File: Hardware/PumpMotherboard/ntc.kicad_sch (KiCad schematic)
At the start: 2 parts, among them J3 T_SENSOR

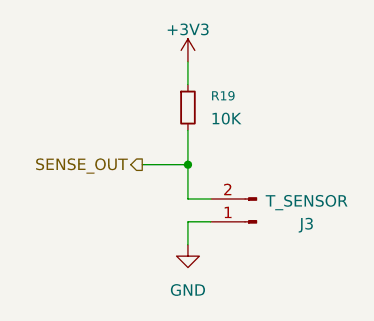
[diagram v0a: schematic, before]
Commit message: Fix DRC and ERC and add AGND
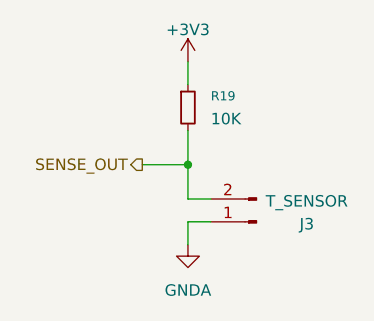
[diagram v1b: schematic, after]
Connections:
- net GND renamed GNDA
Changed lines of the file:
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@@
-	)
-	(symbol
-		(lib_id "power:GND")
-		(at 143.51 118.11 0)
-		(unit 1)
-		(body_style 1)
-		(exclude_from_sim no)
-		(in_bom yes)
-		(on_board yes)
-		(in_pos_files yes)
-		(dnp no)
-		(fields_autoplaced yes)
-		(property "Reference" "#PWR047"
-			(at 143.51 124.46 0)
-			(hide yes)
-			(show_name no)
-			(do_not_autoplace no)
-			(effects
-				(font
-					(size 1.27 1.27)
-				)
-			)
-		)
-		(property "Value" "GND"
-			(at 143.51 123.19 0)
-			(show_name no)
-			(do_not_autoplace no)
-			(effects
-				(font
-					(size 1.27 1.27)
-				)
-			)
-		)
-		(property "Footprint" ""
-			(at 143.51 118.11 0)
-			(hide yes)
-			(show_name no)
-			(do_not_autoplace no)
-			(effects
-				(font
-					(size 1.27 1.27)
-				)
-			)
-		)
-		(property "Datasheet" ""
-			(at 143.51 118.11 0)
-			(hide yes)
-			(show_name no)
-			(do_not_autoplace no)
-			(effects
-				(font
-					(size 1.27 1.27)
-				)
-			)
-		)
-		(property "Description" "Power symbol creates a global label with name \"GND\" , ground"
-			(at 143.51 118.11 0)
-			(hide yes)
-			(show_name no)
-			(do_not_autoplace no)
-			(effects
-				(font
-					(size 1.27 1.27)
-				)
-			)
-		)
-		(pin "1"
-		)
-		(instances
-			(project "PumpMotherboard"
-				(path "/0d3b5c69-c1f2-4eab-9f51-de1d9dac9894/2d92652e-b02e-4262-a61e-86e840250edc"
-					(reference "#PWR047")
-					(unit 1)
-				)
-				(path "/0d3b5c69-c1f2-4eab-9f51-de1d9dac9894/a1739991-ef04-4d0a-bf1d-a4c9667b9ae5"
-					(reference "#PWR050")
-					(unit 1)
-				)
-				(path "/0d3b5c69-c1f2-4eab-9f51-de1d9dac9894/dde12e12-524f-4370-b5e4-73acd2277053"
-					(reference "#PWR052")
-					(unit 1)
-				)
-			)
-		)
 	)
 	(symbol
@@
 					(unit 1)
 				)
+			)
+		)
+	)
+	(symbol
+		(lib_id "power:GNDA")
+		(at 143.51 118.11 0)
+		(unit 1)
+		(body_style 1)
+		(exclude_from_sim no)
+		(in_bom yes)
+		(on_board yes)
+		(in_pos_files yes)
+		(dnp no)
+		(fields_autoplaced yes)
+		(property "Reference" "#PWR047"
+			(at 143.51 124.46 0)
+			(hide yes)
+			(show_name no)
+			(do_not_autoplace no)
+			(effects
+				(font
+					(size 1.27 1.27)
+				)
+			)
+		)
+		(property "Value" "GNDA"
+			(at 143.51 123.19 0)
+			(show_name no)
+			(do_not_autoplace no)
+			(effects
+				(font
+					(size 1.27 1.27)
+				)
+			)
+		)
+		(property "Footprint" ""
+			(at 143.51 118.11 0)
+			(hide yes)
+			(show_name no)
+			(do_not_autoplace no)
+			(effects
+				(font
+					(size 1.27 1.27)
+				)
+			)
+		)
+		(property "Datasheet" ""
+			(at 143.51 118.11 0)
+			(hide yes)
+			(show_name no)
+			(do_not_autoplace no)
+			(effects
+				(font
+					(size 1.27 1.27)
+				)
+			)
+		)
+		(property "Description" "Power symbol creates a global label with name \"GNDA\" , analog ground"
+			(at 143.51 118.11 0)
+			(hide yes)
+			(show_name no)
+			(do_not_autoplace no)
+			(effects
+				(font
+					(size 1.27 1.27)
+				)
+			)
+		)
+		(pin "1"
+		)
+		(instances
+			(project "PumpMotherboard"
+				(path "/0d3b5c69-c1f2-4eab-9f51-de1d9dac9894/2d92652e-b02e-4262-a61e-86e840250edc"
+					(reference "#PWR047")
+					(unit 1)
+				)
+				(path "/0d3b5c69-c1f2-4eab-9f51-de1d9dac9894/a1739991-ef04-4d0a-bf1d-a4c9667b9ae5"
+					(reference "#PWR050")
+					(unit 1)
+				)
+				(path "/0d3b5c69-c1f2-4eab-9f51-de1d9dac9894/dde12e12-524f-4370-b5e4-73acd2277053"
+					(reference "#PWR052")
+					(unit 1)
+				)
